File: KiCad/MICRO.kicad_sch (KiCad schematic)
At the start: 15 parts, among them J2 DE9_Pins, J4 DE9_Pins, J8 Conn_PIC_ICSP_ICD, U2 SN65HVD232, U7 PIC32MX250F128D-IPT, Y1 Crystal

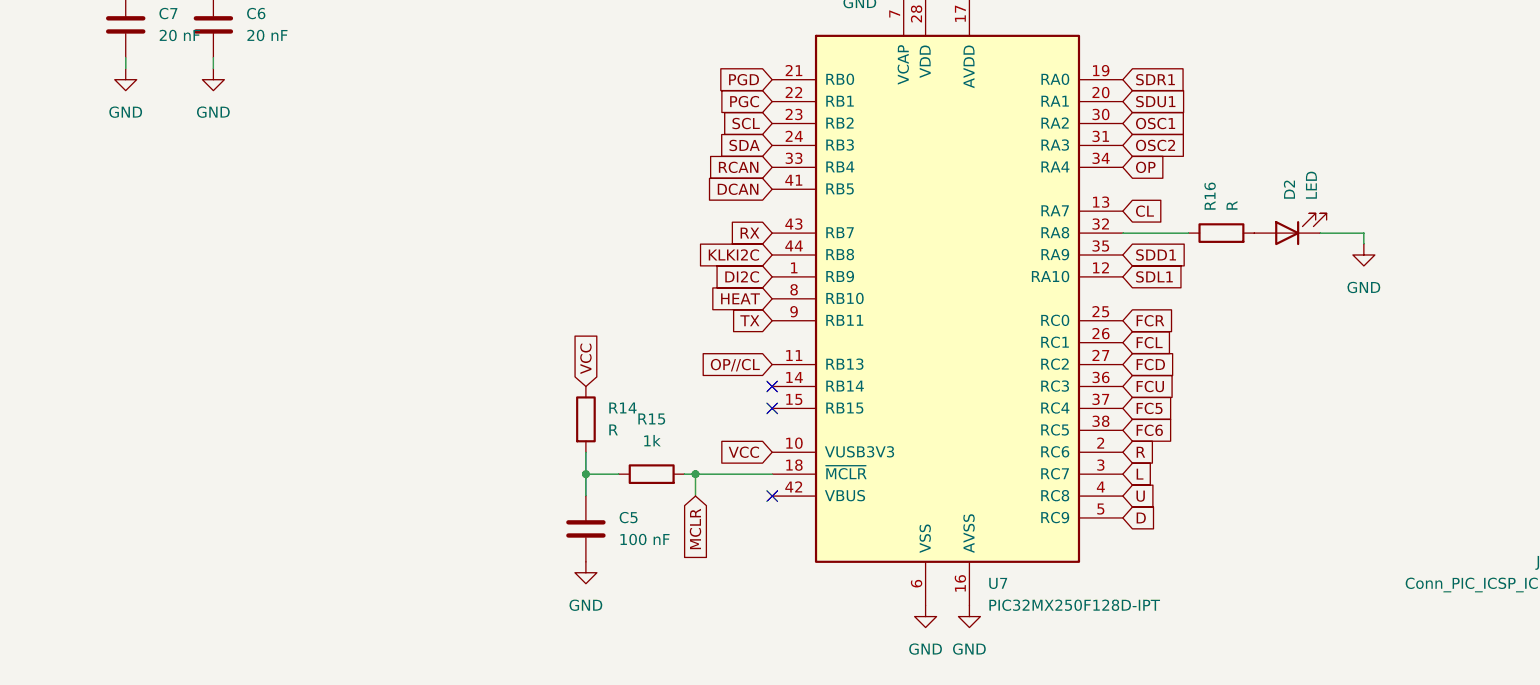
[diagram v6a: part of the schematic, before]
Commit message: cambiado layout general
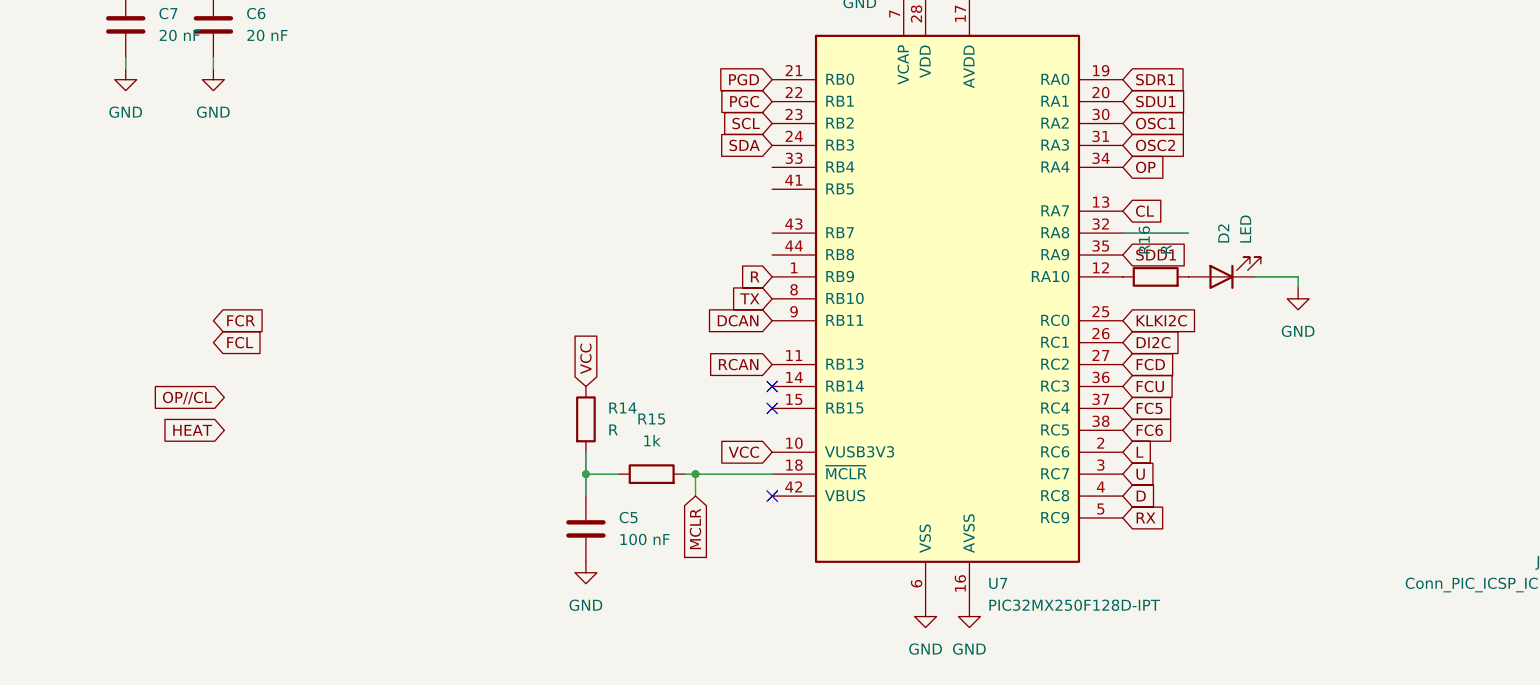
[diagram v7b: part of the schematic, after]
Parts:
- J2, J4: footprint Connector_Dsub:DSUB-9_Pins_Vertical_P2.77x2.84mm -> Connector_Dsub:DSUB-9_Pins_Horizontal_P2.77x2.84mm_EdgePinOffset9.90mm_Housed_MountingHolesOffset11.32mm
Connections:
- net SDL1 is gone; now on an unnamed net: U7.12 (RA10)
- net D: now also U7.4 (RC8); no longer U7.5 (RC9)
- net DCAN: now also U7.9 (RB11); no longer U7.41 (RB5)
- net DI2C: now also U7.26 (RC1); no longer U7.1 (RB9)
- net FCL: no longer U7.26 (RC1)
- net FCR: no longer U7.25 (RC0)
- net HEAT: no longer U7.8 (RB10)
- net KLKI2C: now also U7.25 (RC0); no longer U7.44 (RB8)
- net L: now also U7.2 (RC6); no longer U7.3 (RC7)
- net OP//CL: no longer U7.11 (RB13)
- net R: now also U7.1 (RB9); no longer U7.2 (RC6)
- net RCAN: now also U7.11 (RB13); no longer U7.33 (RB4)
- net RX: now also U7.5 (RC9); no longer U7.43 (RB7)
- net TX: now also U7.8 (RB10); no longer U7.9 (RB11)
- net U: now also U7.3 (RC7); no longer U7.4 (RC8)
- net at R16.1: no longer U7.32 (RA8)
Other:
- moved on the sheet: D2, R16

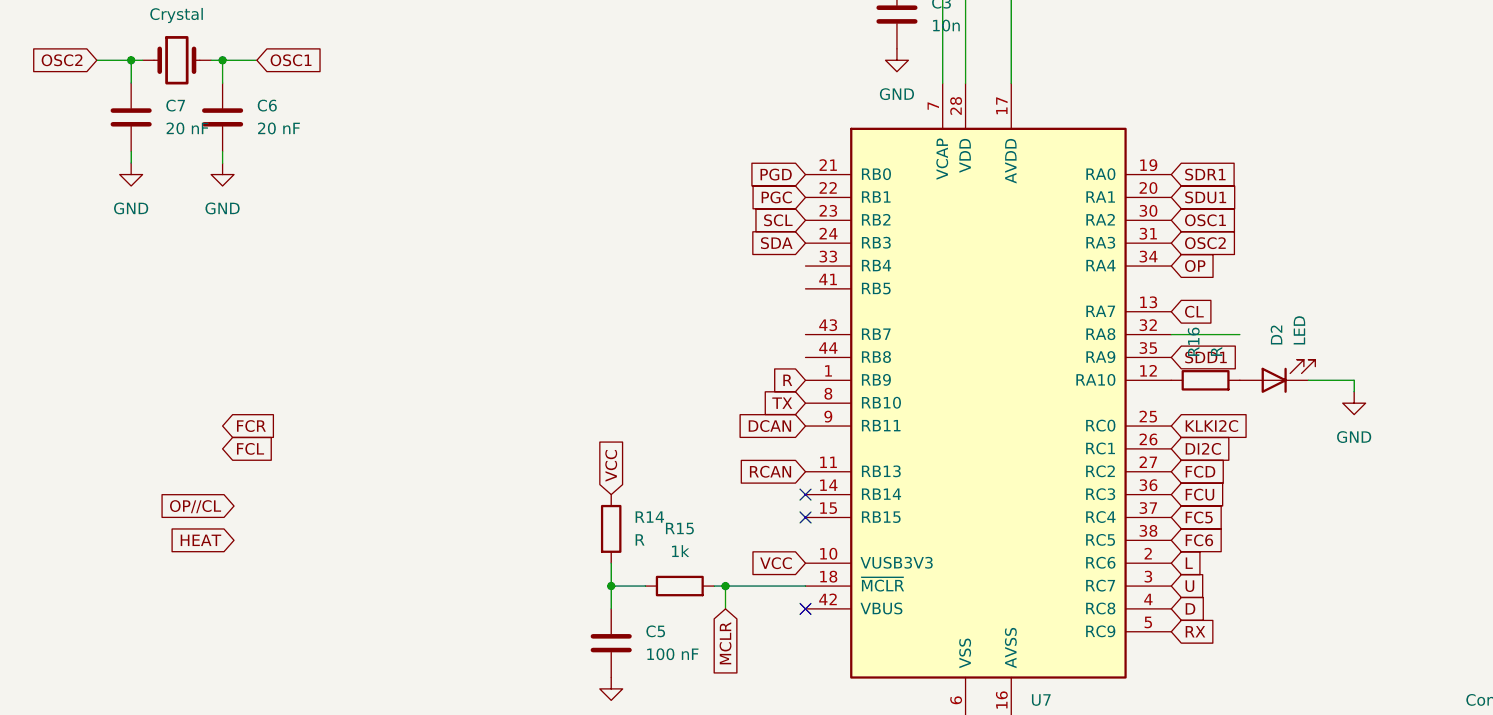
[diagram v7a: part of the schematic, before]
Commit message: terminado placement (reorganizado pines del micro y añadido cambios de sensores/calefactor por conectores)
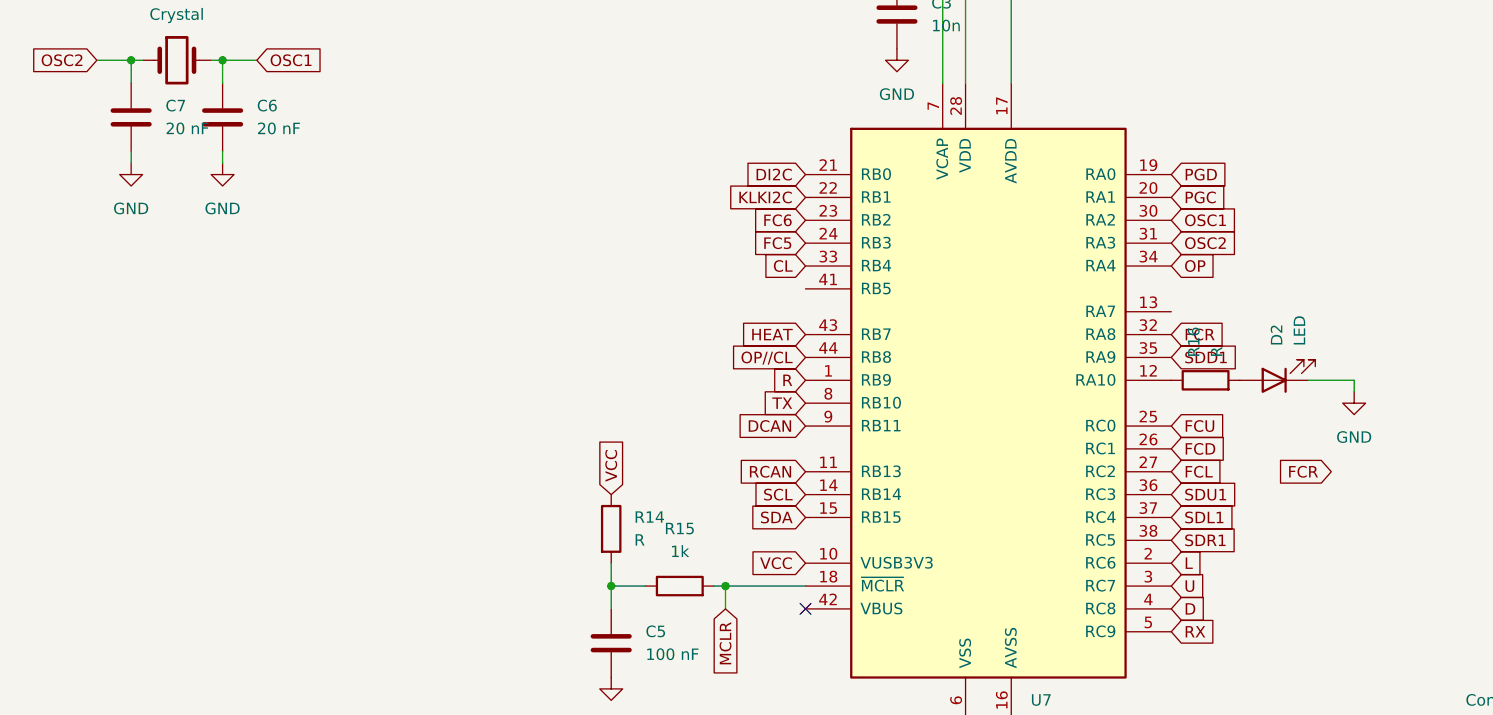
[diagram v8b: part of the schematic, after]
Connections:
- net CL: now also U7.33 (RB4); no longer U7.13 (RA7)
- net DI2C: now also U7.21 (RB0); no longer U7.26 (RC1)
- net FC5: now also U7.24 (RB3); no longer U7.37 (RC4)
- net FC6: now also U7.23 (RB2); no longer U7.38 (RC5)
- net FCD: now also U7.26 (RC1); no longer U7.27 (RC2)
- net FCL: now also U7.27 (RC2)
- net FCR: now also U7.32 (RA8)
- net FCU: now also U7.25 (RC0); no longer U7.36 (RC3)
- net HEAT: now also U7.43 (RB7)
- net KLKI2C: now also U7.22 (RB1); no longer U7.25 (RC0)
- net OP//CL: now also U7.44 (RB8)
- net PGC: now also U7.20 (RA1); no longer U7.22 (RB1)
- net PGD: now also U7.19 (RA0); no longer U7.21 (RB0)
- net SCL: now also U7.14 (RB14); no longer U7.23 (RB2)
- net SDA: now also U7.15 (RB15); no longer U7.24 (RB3)
- net SDR1: now also U7.38 (RC5); no longer U7.19 (RA0)
- net SDU1: now also U7.36 (RC3); no longer U7.20 (RA1)
- new net SDL1: U7.37 (RC4)
- no-connect marks 18 -> 16
